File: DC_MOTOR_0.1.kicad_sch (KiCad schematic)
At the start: 17 parts, among them P10 Pad, P11 Pad, U2 TLE9201SG

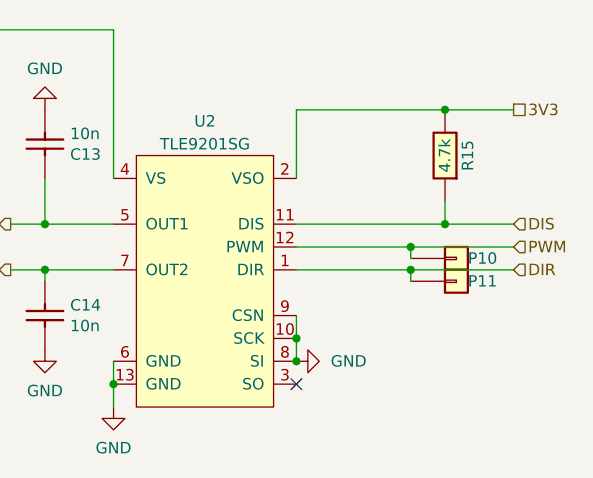
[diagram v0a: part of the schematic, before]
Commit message: colocacion de los componentes en un 90%
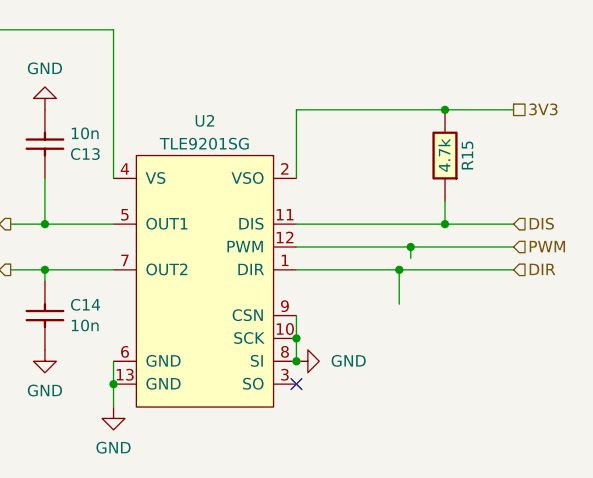
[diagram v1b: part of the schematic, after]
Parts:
- removed P10, P11: Pad, hellen-one-common:PAD-TH, symbol hellen-one-common:Pad
